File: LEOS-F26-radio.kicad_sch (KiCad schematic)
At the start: 1 part

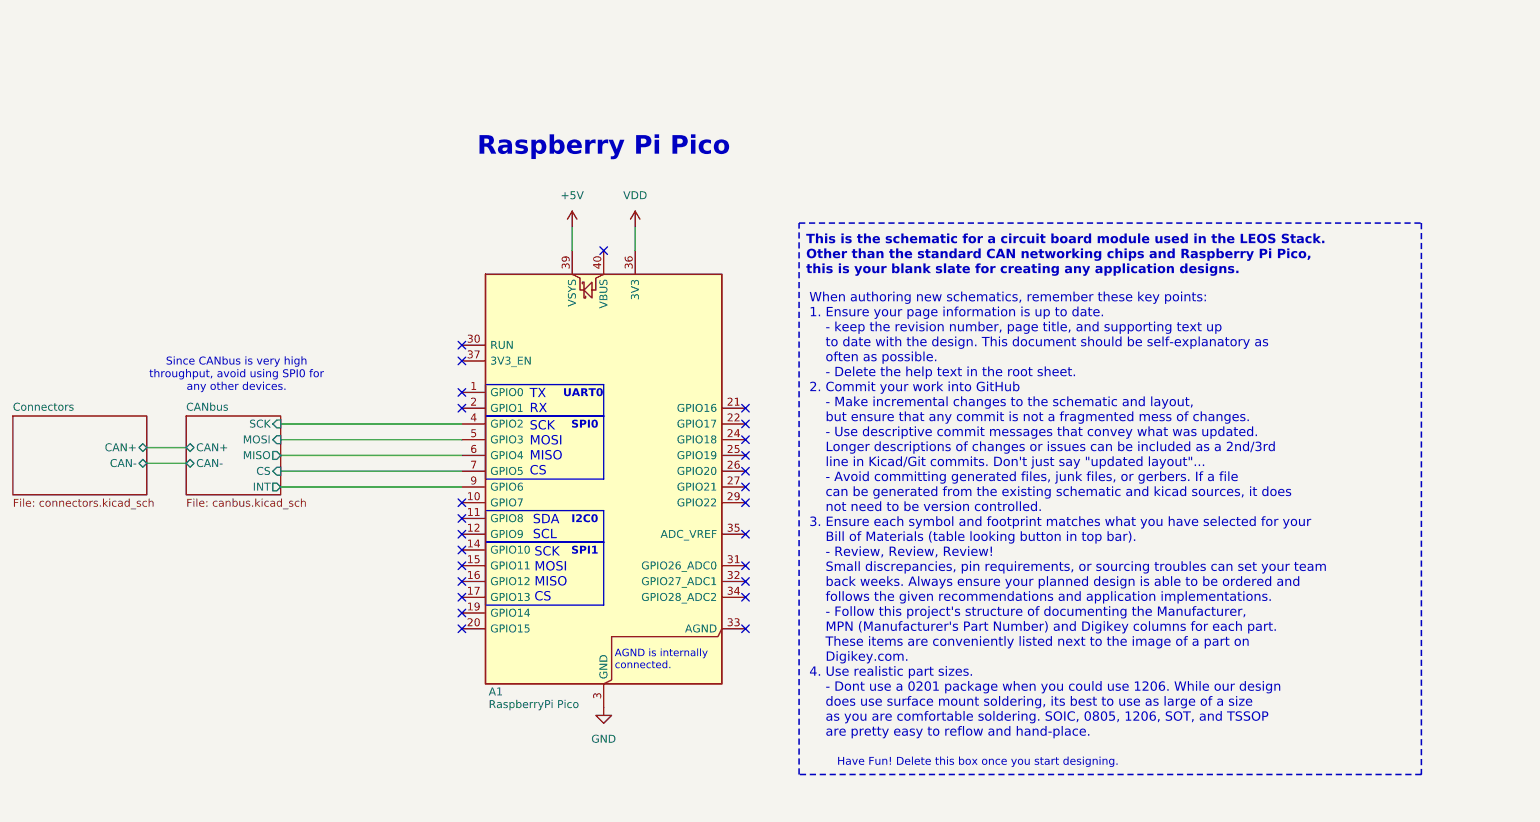
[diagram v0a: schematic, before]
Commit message: schematic and routing updated
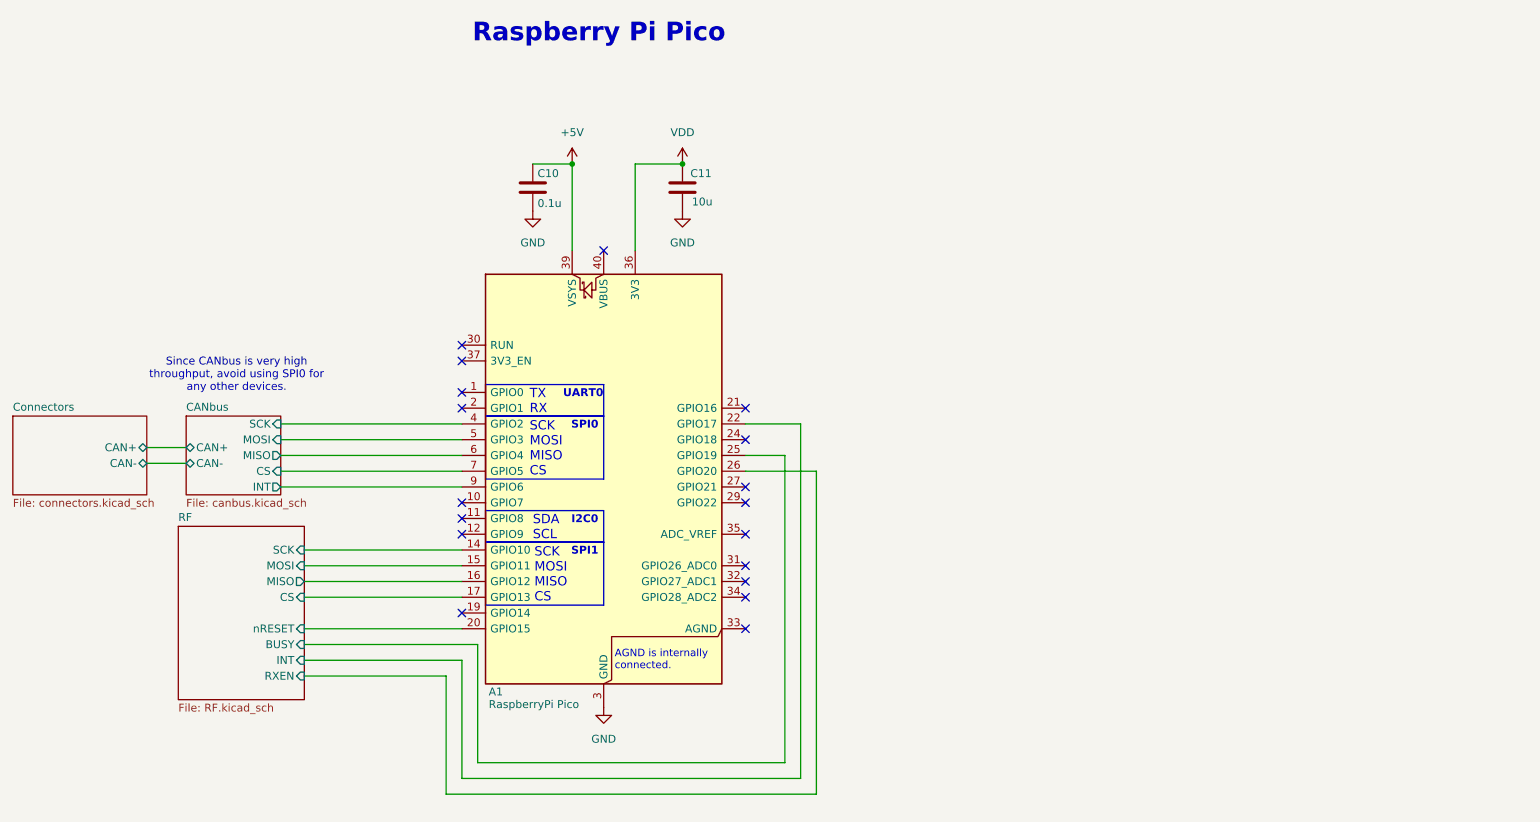
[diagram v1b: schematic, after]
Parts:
- added C10: 0.1u, Capacitor_SMD:C_0805_2012Metric, symbol Device:C
- added C11: 10u, Capacitor_SMD:C_0805_2012Metric, symbol Device:C
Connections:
- net +5V: now also C10.1
- net GND: now also C10.2, C11.2
- net VDD: now also C11.1
- net RF/SCK: now reaches A1.14 (GPIO10)
- net RF/MOSI: now reaches A1.15 (GPIO11)
- net RF/MISO: now reaches A1.16 (GPIO12)
- net RF/CS: now reaches A1.17 (GPIO13)
- net RF/nRESET: now reaches A1.20 (GPIO15)
- net RF/INT: now reaches A1.22 (GPIO17)
- net RF/BUSY: now reaches A1.25 (GPIO19)
- net RF/RXEN: now reaches A1.26 (GPIO20)
- no-connect marks 26 -> 18
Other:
- added sheet RF (RF.kicad_sch)
- note removed: "Have Fun! Delete this box once you start designing."
- note removed: "This is the schematic for a circuit board module used in the LEOS Stack. Other than the standard CAN networking chips and Raspberry Pi Pico, this is your blank slate for creating any application designs."
- note removed: "When authoring new schematics, remember these key points: 1. Ensure your page information is up to date. - keep the revision number, page title, and supporting text up to date with the design. This document should be self-explanatory as often as possible. - Delete the help text in the root sheet. 2. Commit your work into GitHub - Make incremental changes to the schematic and layout, but ensure th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"
- title: LEOS Microcontroller -> LEOS Radio

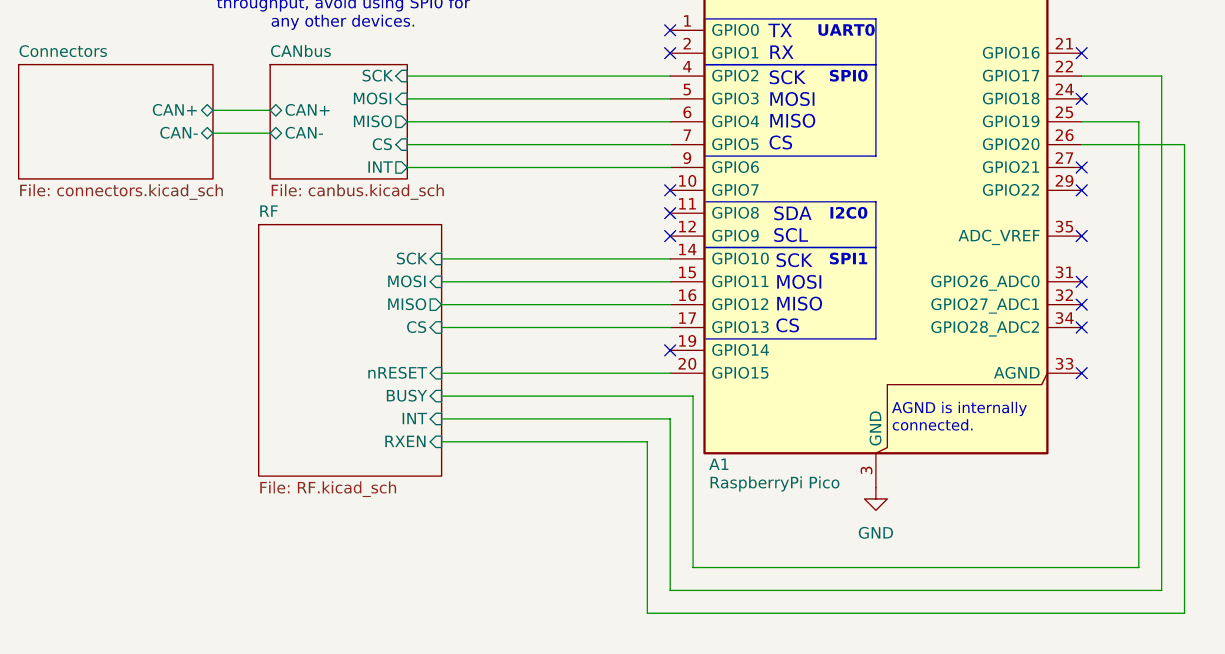
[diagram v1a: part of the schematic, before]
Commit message: Change radio reset pullup to IO voltage, fix net labels
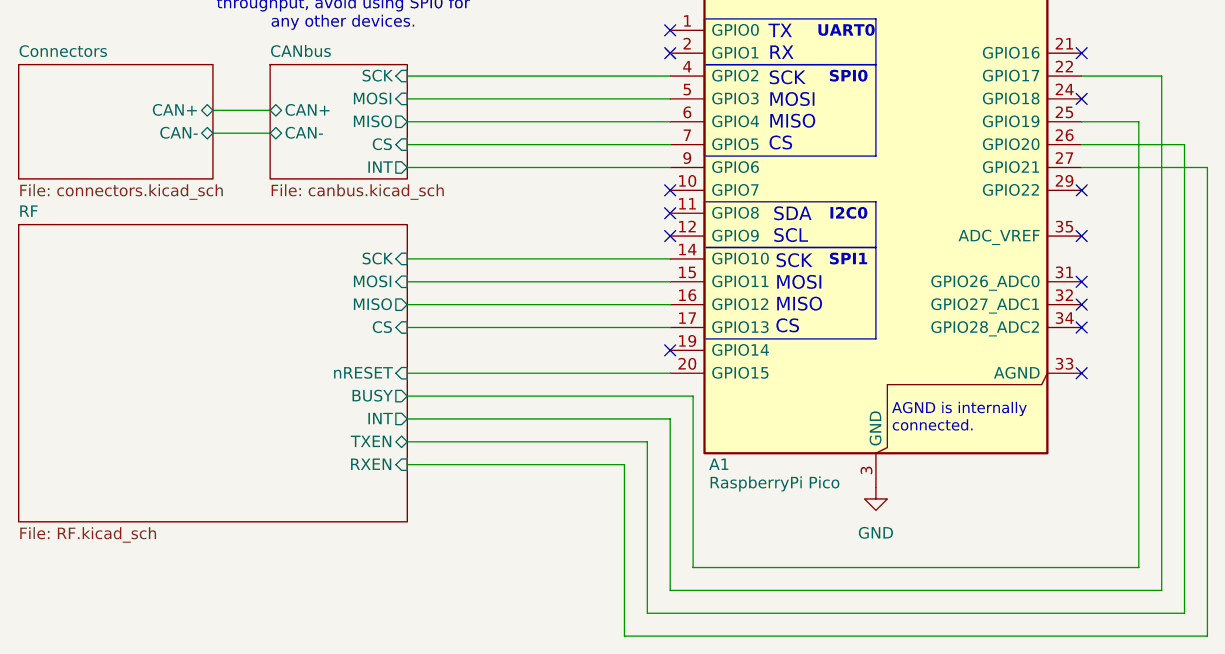
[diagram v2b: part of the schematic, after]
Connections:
- net RF/RXEN: now also A1.27 (GPIO21); no longer A1.26 (GPIO20)
- new net RF/TXEN: A1.26 (GPIO20)
- no-connect marks 18 -> 17
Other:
- sheet RF ports: added TXEN; removed none
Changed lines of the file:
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@@
 		(title "LEOS Radio")
 		(date "2026-10-05")
-		(rev "1.0")
+		(rev "2.1")
 		(company "VIP Lightning From the Edge of Space")
 	)
@@
 	)
 	(no_connect
-		(at 170.18 104.14)
-	)
-	(no_connect
 		(at 170.18 111.76)
 	)
@@
 	(wire
 		(pts
+			(xy 184.15 104.14) (xy 170.18 104.14)
+		)
+		(stroke
+			(width 0)
+			(type default)
+		)
+	)
+	(wire
+		(pts
 			(xy 95.25 101.6) (xy 124.46 101.6)
 		)
@@
 	(wire
 		(pts
-			(xy 99.06 114.3) (xy 124.46 114.3)
+			(xy 95.25 114.3) (xy 124.46 114.3)
 		)
 		(stroke
@@
 	(wire
 		(pts
-			(xy 99.06 134.62) (xy 121.92 134.62)
+			(xy 95.25 134.62) (xy 121.92 134.62)
+		)
+		(stroke
+			(width 0)
+			(type default)
+		)
+	)
+	(wire
+		(pts
+			(xy 184.15 156.21) (xy 184.15 104.14)
 		)
 		(stroke
@@
 	(wire
 		(pts
-			(xy 99.06 132.08) (xy 124.46 132.08)
-		)
-		(stroke
-			(width 0)
-			(type default)
-		)
-	)
-	(wire
-		(pts
-			(xy 99.06 121.92) (xy 124.46 121.92)
+			(xy 95.25 132.08) (xy 124.46 132.08)
+		)
+		(stroke
+			(width 0)
+			(type default)
+		)
+	)
+	(wire
+		(pts
+			(xy 95.25 121.92) (xy 124.46 121.92)
 		)
 		(stroke
@@
 	(wire
 		(pts
-			(xy 99.06 129.54) (xy 127 129.54)
+			(xy 95.25 129.54) (xy 127 129.54)
 		)
 		(stroke
@@
 	(wire
 		(pts
+			(xy 119.38 137.16) (xy 119.38 156.21)
+		)
+		(stroke
+			(width 0)
+			(type default)
+		)
+	)
+	(wire
+		(pts
 			(xy 73.66 100.33) (xy 80.01 100.33)
 		)
@@
 	(wire
 		(pts
-			(xy 99.06 127) (xy 124.46 127)
+			(xy 95.25 127) (xy 124.46 127)
 		)
 		(stroke
@@
 	(wire
 		(pts
-			(xy 99.06 119.38) (xy 124.46 119.38)
+			(xy 95.25 119.38) (xy 124.46 119.38)
 		)
 		(stroke
@@
 	(wire
 		(pts
-			(xy 99.06 116.84) (xy 124.46 116.84)
+			(xy 119.38 156.21) (xy 184.15 156.21)
+		)
+		(stroke
+			(width 0)
+			(type default)
+		)
+	)
+	(wire
+		(pts
+			(xy 95.25 116.84) (xy 124.46 116.84)
 		)
 		(stroke
@@
 		(pts
 			(xy 95.25 93.98) (xy 124.46 93.98)
+		)
+		(stroke
+			(width 0)
+			(type default)
+		)
+	)
+	(wire
+		(pts
+			(xy 95.25 137.16) (xy 119.38 137.16)
 		)
 		(stroke
@@
 	)
 	(sheet
-		(at 78.74 110.49)
-		(size 20.32 27.94)
+		(at 52.07 110.49)
+		(size 43.18 33.02)
 		(exclude_from_sim no)
 		(in_bom yes)
@@
 		)
 		(property "Sheetname" "RF"
-			(at 78.74 109.7784 0)
+			(at 52.07 109.7784 0)
 			(show_name no)
 			(do_not_autoplace no)
@@
 		)
 		(property "Sheetfile" "RF.kicad_sch"
-			(at 78.74 139.0146 0)
+			(at 52.07 144.0946 0)
 			(show_name no)
 			(do_not_autoplace no)
@@
 			)
 		)
-		(pin "BUSY" input
-			(at 99.06 129.54 0)
+		(pin "BUSY" output
+			(at 95.25 129.54 0)
 			(effects
 				(font
@@
 		)
 		(pin "CS" input
-			(at 99.06 121.92 0)
+			(at 95.25 121.92 0)
 			(effects
 				(font
@@
 			)
 		)
-		(pin "INT" input
-			(at 99.06 132.08 0)
+		(pin "INT" output
+			(at 95.25 132.08 0)
 			(effects
 				(font
@@
 		)
 		(pin "MISO" output
-			(at 99.06 119.38 0)
+			(at 95.25 119.38 0)
 			(effects
 				(font
@@
 		)
 		(pin "MOSI" input
-			(at 99.06 116.84 0)
+			(at 95.25 116.84 0)
 			(effects
 				(font
@@
 		)
 		(pin "nRESET" input
-			(at 99.06 127 0)
+			(at 95.25 127 0)
 			(effects
 				(font
@@
 		)
 		(pin "RXEN" input
-			(at 99.06 134.62 0)
+			(at 95.25 137.16 0)
 			(effects
 				(font
@@
 		)
 		(pin "SCK" input
-			(at 99.06 114.3 0)
-			(effects
-				(font
+			(at 95.25 114.3 0)
+			(effects
+				(font
+					(size 1.27 1.27)
+				)
+				(justify right)
+			)
+		)
+		(pin "TXEN" bidirectional
+			(at 95.25 134.62 0)
+			(effects
+				(font
